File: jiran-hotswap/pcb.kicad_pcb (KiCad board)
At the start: 2 copper layers, 152.3 x 104.7 mm, 105 parts, among them J1 TRRS, SW1 SW_Push, SW10 SW_Push, SW11 SW_Push, SW12 SW_Push, SW13 SW_Push, SW14 SW_Push, SW15 SW_Push, SW16 SW_Push, SW17 SW_Push, SW18 SW_Push, SW19 SW_Push, SW2 SW2, SW20 SW_Push, SW21 SW_Push, SW22 SW_Push, SW23 SW_Push, SW24 SW_Push, SW25 SW_Push, SW26 SW_Push, SW27 SW_Push, SW28 SW_Push, SW29 SW_Push, SW3 SW_Push, SW4 SW_Push, SW5 SW_Push, SW6 SW_Push, SW7 SW_Push, SW8 SW_Push, SW9 SW_Push, U1 ProMicro

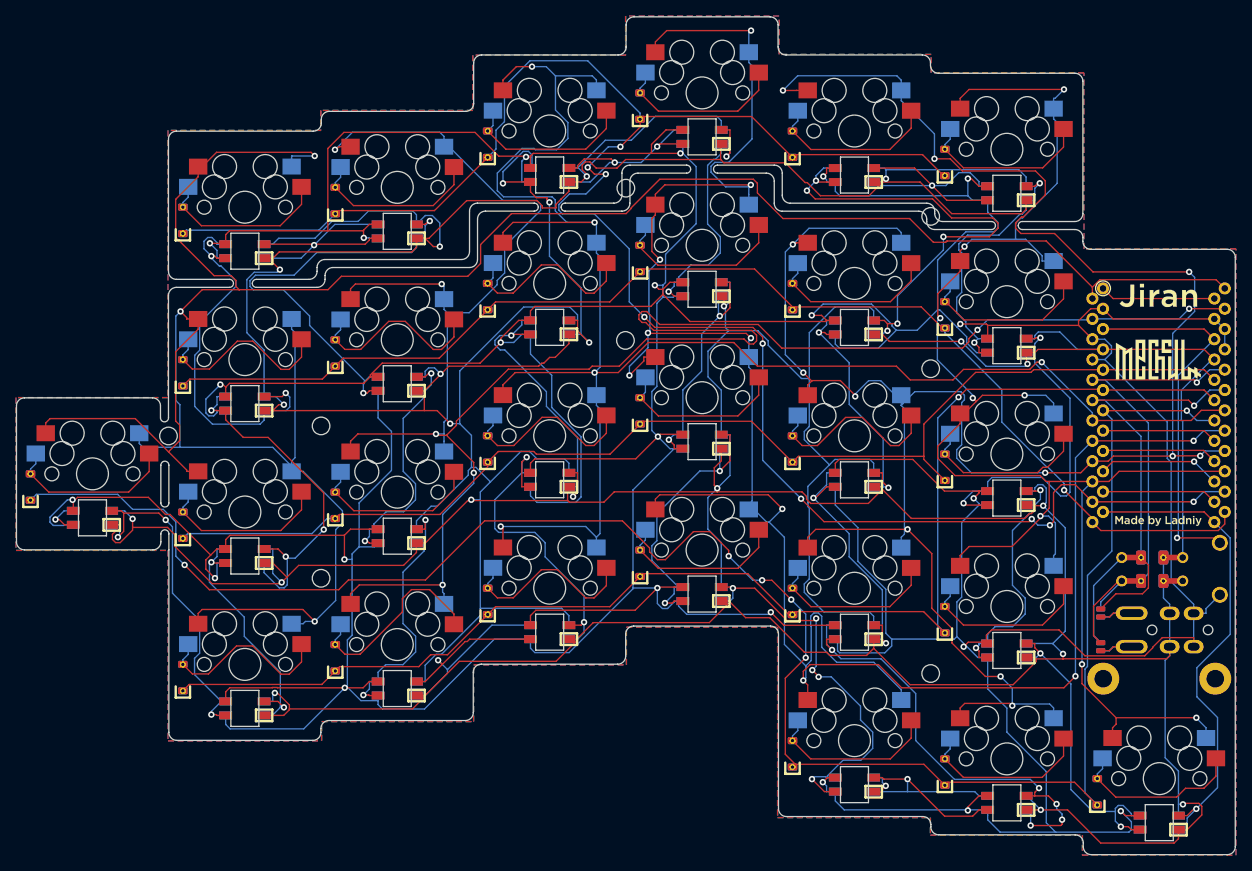
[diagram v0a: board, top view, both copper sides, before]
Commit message: Remove tracks from PCb
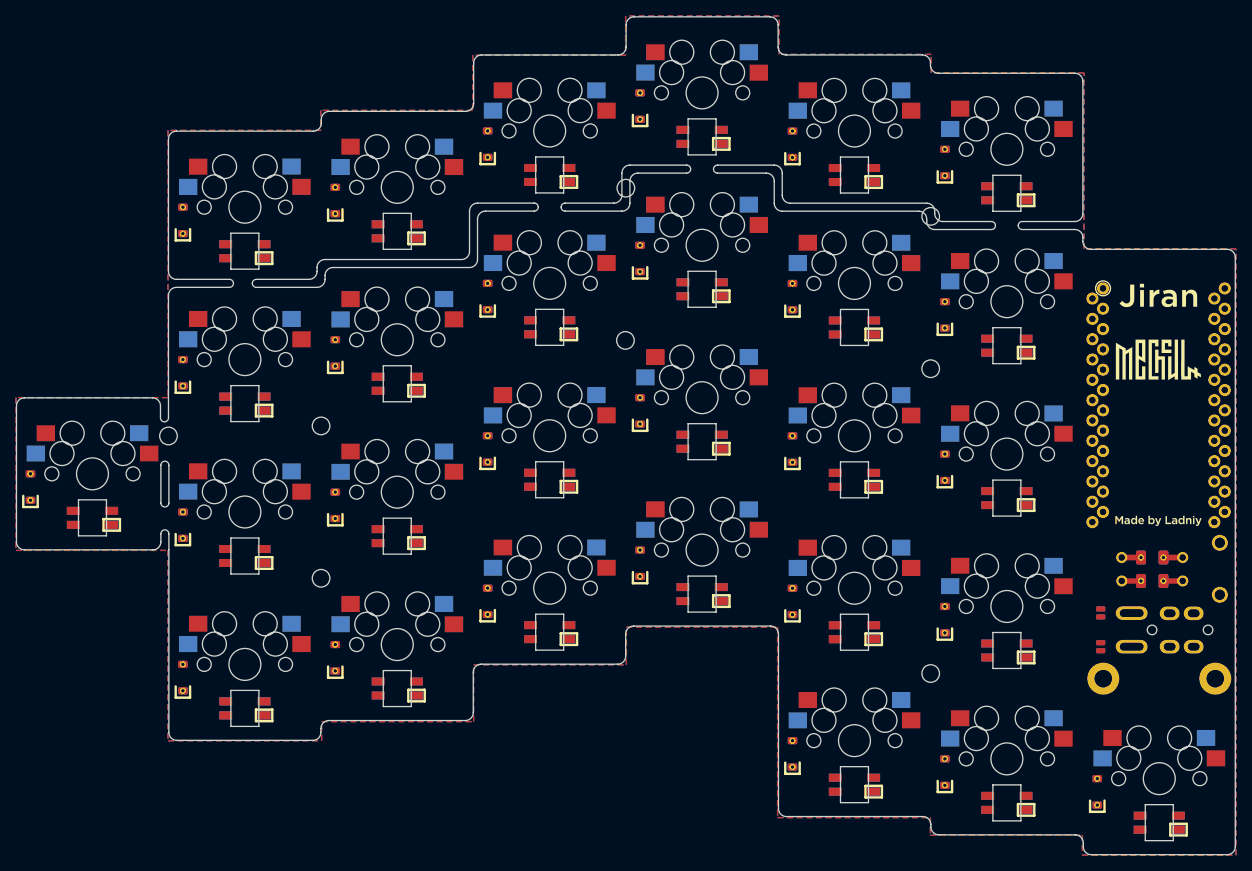
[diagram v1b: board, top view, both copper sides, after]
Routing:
- net VCC: track 983.3 -> 0.00 mm, vias 19 -> 0
- net GND: track 949.0 -> 0.00 mm, vias 23 -> 0
- net /col0: track 334.9 -> 0.00 mm, vias 3 -> 0
- net /col4: track 284.5 -> 0.00 mm, vias 12 -> 0
- net /col1: track 278.8 -> 0.00 mm, vias 7 -> 0
- net /col3: track 278.5 -> 0.00 mm, vias 10 -> 0
- net /rowA: track 253.9 -> 0.00 mm, vias 9 -> 0
- net /rowE: track 243.9 -> 0.00 mm, vias 6 -> 0
- net /col2: track 222.5 -> 0.00 mm, vias 5 -> 0
- net /col5: track 205.2 -> 0.00 mm, vias 8 -> 0
- net /rowD: track 168.6 -> 0.00 mm, vias 1 -> 0
- net /rowB: track 155.5 -> 0.00 mm, vias 1 -> 0
- net /rowC: track 149.5 -> 0.00 mm
- net SCL: track 66.9 -> 0.00 mm, vias 1 -> 0
- net SDA: track 63.5 -> 0.00 mm, vias 1 -> 0
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
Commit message: Remove RGB leds footprints
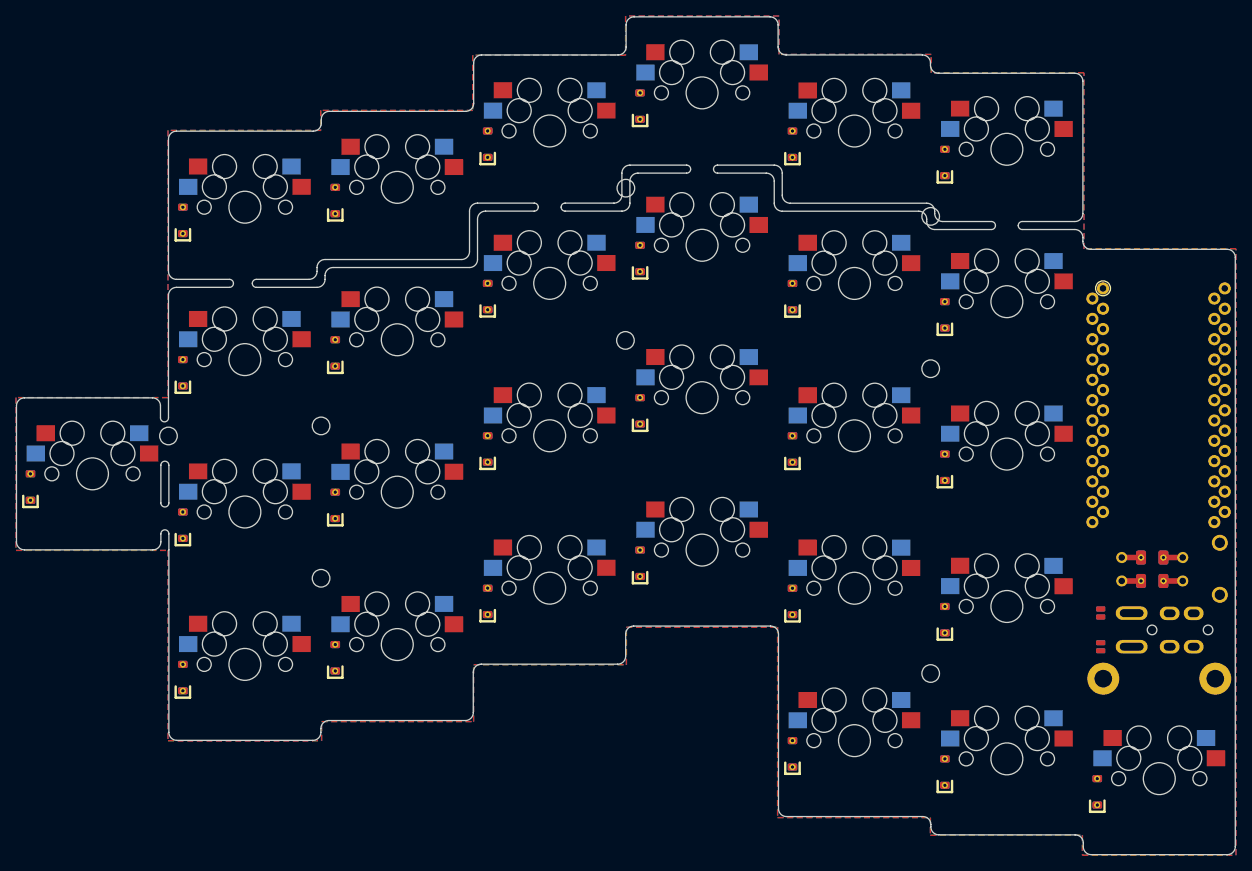
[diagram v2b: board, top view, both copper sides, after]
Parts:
- removed L1, L10, L11, L12, L13, L14, L15, L16, L17, L18, L19, L2, L20, L21, L22, L23, L24, L25, L26, L27, L28, L3, L4, L5, L6, L7, L8, L9: SK6812MINI-kbd, Used_Footprints:SK6812MINI
- removed LG1, LG2: Silk_Logo_New, Used_Footprints:Silk_Logo_New
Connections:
- U1 pad 13: /RGB -> Net-(U1-Pad13)
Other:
- outline, holes or cut-outs redrawn

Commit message: Add logos
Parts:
- added LG1: Silk_Logo_New, Used_Footprints:Silk_Logo_New, F.Cu at (206.2, 84.4)
- added LG2: Silk_Logo_New, Used_Footprints:Silk_Logo_New, B.Cu at (206.2, 84.4)

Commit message: Route tracks
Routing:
- net /col0: track 0.00 -> 319.3 mm, vias 0 -> 1
- net /col1: track 0.00 -> 248.1 mm, vias 0 -> 2
- net /col3: track 0.00 -> 244.6 mm, vias 0 -> 3
- net /col4: track 0.00 -> 234.7 mm, vias 0 -> 5
- net /rowE: track 0.00 -> 229.9 mm, vias 0 -> 1
- net /col2: track 0.00 -> 216.5 mm, vias 0 -> 2
- net /col5: track 0.00 -> 200.4 mm, vias 0 -> 4
- net /rowD: track 0.00 -> 179.8 mm, vias 0 -> 1
- net /rowA: track 0.00 -> 178.1 mm
- net /rowB: track 0.00 -> 164.2 mm
- net /rowC: track 0.00 -> 148.2 mm
- net GND: track 0.00 -> 71.6 mm
- net SDA: track 0.00 -> 64.3 mm, vias 0 -> 1
- net VCC: track 0.00 -> 60.2 mm
- net SCL: track 0.00 -> 59.4 mm, vias 0 -> 1
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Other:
- net class Default: trace_width 0.17 -> 0.2
